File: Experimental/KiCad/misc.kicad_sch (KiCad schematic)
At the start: 72 parts, among them IC6 SN74LVC1G14DBVR, IC7 TPS62933ODRLR, IC8 TPS62933ODRLR, Q4 MMBT5401, Q5 2N7002, Q6 DMP3013SFV-7, Q7 DMP3013SFV-7, SW1 WBL2UOAGQR05CLR, SW2 LP4EE1RBATY, SW3 PEC16-2215F-S0024, X3 571-0400, X4 GSP1.9101.1, X5 PJ-002BH-SMT-TR

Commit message: BOM update, small changes
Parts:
- C22: TME R46KI310000M1M -> MKPX2-100NR15
- R34: TME SMD0603-3K3-1% -> SMD0603-200K-1%
- renumbered D9 to D10, D10 to D9, JP12 to JP13, R40 to R38, R38 to R39, R39 to R40
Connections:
- net +12P: now also D10.C
- net at C23.1, L1.1, TR1.V+ (+): no longer D10.C
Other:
- moved on the sheet: C32, D10, Q7, R38, X5, ZD2

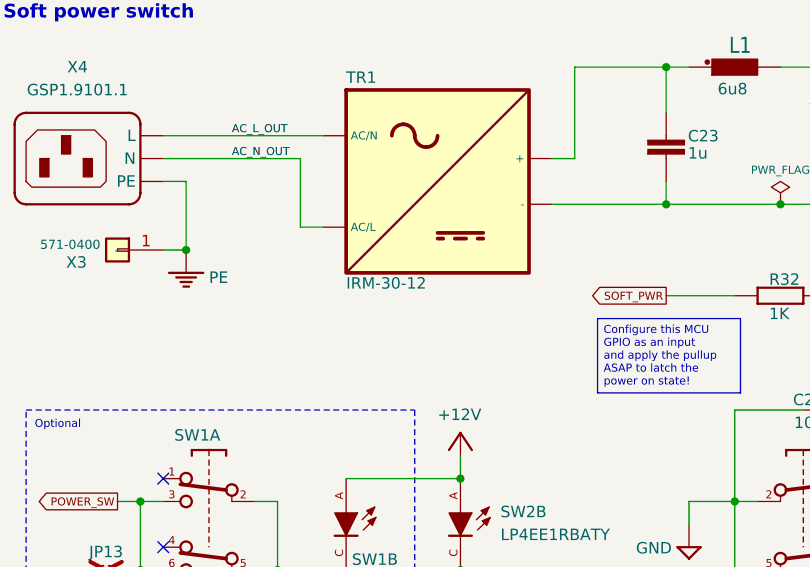
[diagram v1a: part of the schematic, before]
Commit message: AC/DC module replaced with 45/60W model
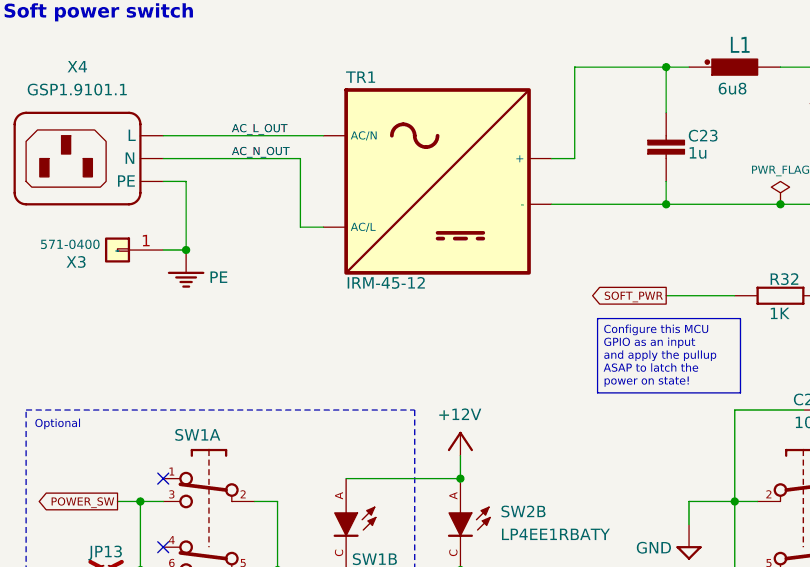
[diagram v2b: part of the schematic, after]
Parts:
- TR1: value IRM-30-12 -> IRM-45-12; footprint PCM_EEZ_THT:IRM-30 -> PCM_EEZ_THT:IRM-45; DigiKey 1866-3043-ND -> 1866-3053-ND; LCSC C193294 -> C5772350; Mouser 709-IRM30-12 -> 709-IRM45-12; TME IRM-30-12 -> IRM-45-12
- X5: Label (none) -> 12Vdc
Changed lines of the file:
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@@
+			)
+		)
+		(property "Label" "12Vdc"
+			(at 160.02 99.06 0)
+			(effects
+				(font
+					(size 0.889 0.889)
+				)
+				(hide yes)
 			)
 		)
@@
 			)
 		)
-		(property "Value" "IRM-30-12"
+		(property "Value" "IRM-45-12"
 			(at 53.34 47.625 0)
 			(effects
@@
 			)
 		)
-		(property "Footprint" "PCM_EEZ_THT:IRM-30"
+		(property "Footprint" "PCM_EEZ_THT:IRM-45"
 			(at 63.5 35.56 0)
 			(effects
@@
 			)
 		)
-		(property "DigiKey" "1866-3043-ND"
-			(at 63.5 35.56 0)
-			(effects
-				(font
-					(size 1.27 1.27)
-				)
-				(hide yes)
-			)
-		)
-		(property "Mouser" "709-IRM30-12"
-			(at 63.5 35.56 0)
-			(effects
-				(font
-					(size 1.27 1.27)
-				)
-				(hide yes)
-			)
-		)
-		(property "TME" "IRM-30-12"
-			(at 63.5 35.56 0)
-			(effects
-				(font
-					(size 1.27 1.27)
-				)
-				(hide yes)
-			)
-		)
-		(property "LCSC" "C193294"
-			(at 63.5 35.56 0)
-			(effects
+		(property "DigiKey" "1866-3053-ND"
+			(at 63.5 35.56 0)
+			(effects
+				(font
+					(size 1.27 1.27)
+				)
+				(hide yes)
+			)
+		)
+		(property "Mouser" "709-IRM45-12"
+			(at 63.5 35.56 0)
+			(effects
+				(font
+					(size 1.27 1.27)
+				)
+				(hide yes)
+			)
+		)
+		(property "TME" "IRM-45-12"
+			(at 63.5 35.56 0)
+			(effects
+				(font
+					(size 1.27 1.27)
+				)
+				(hide yes)
+			)
+		)
+		(property "LCSC" "C5772350"
+			(at 63.5 35.56 0)
+			(effects

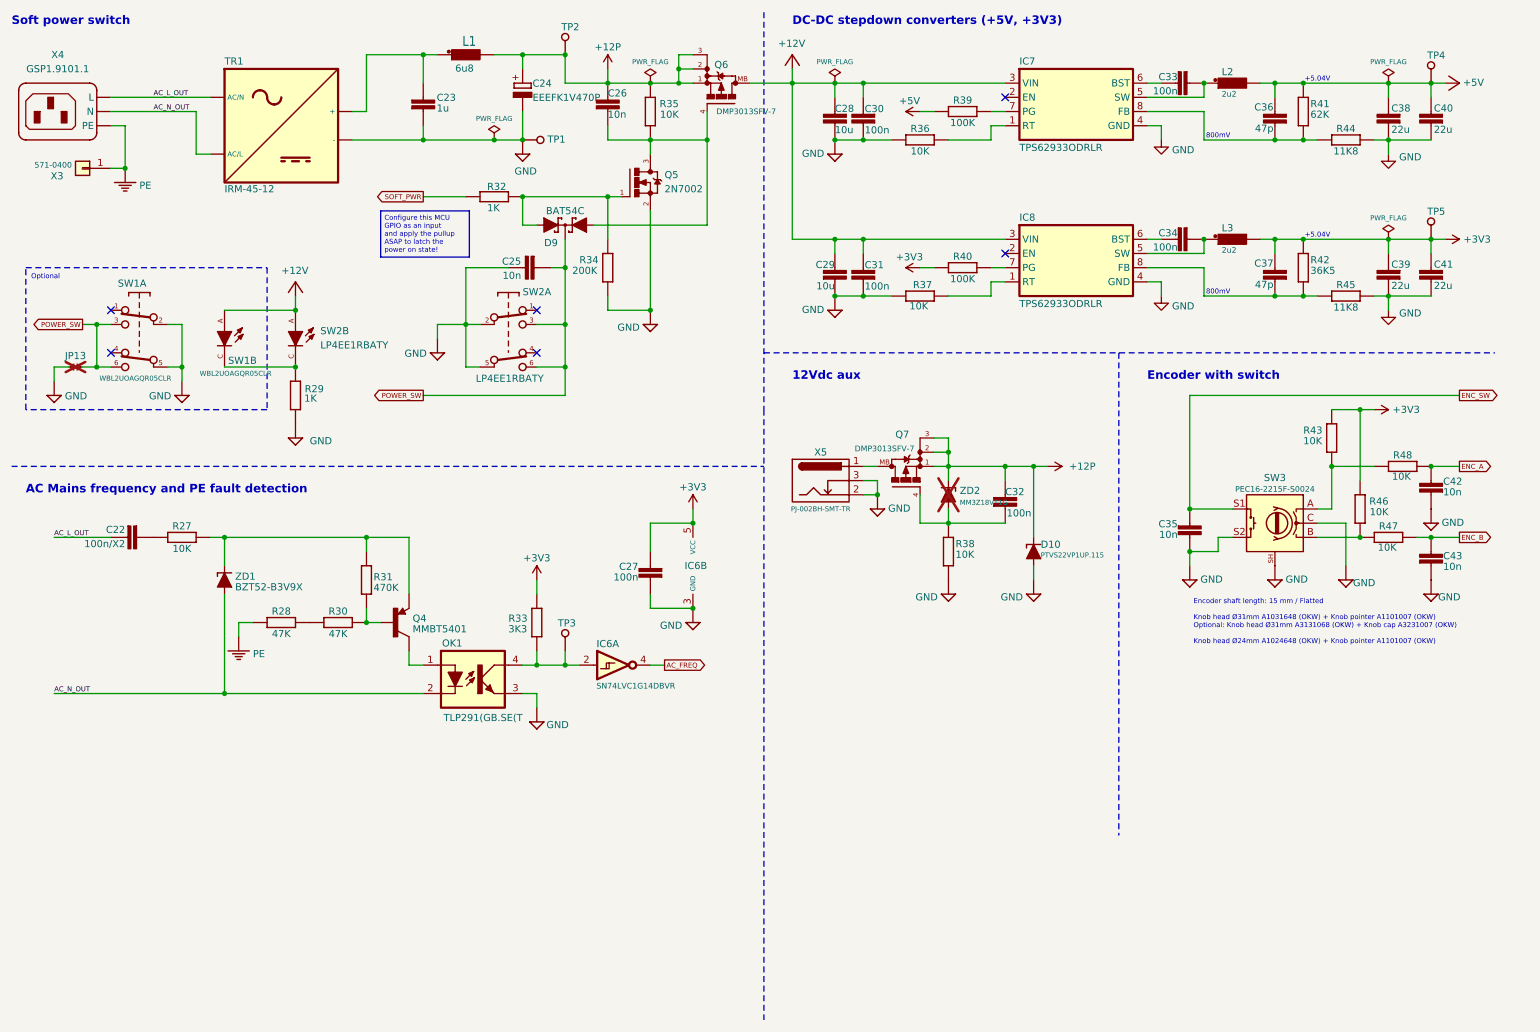
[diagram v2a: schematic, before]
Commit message: Replace 5V buck with 6A low EMI version
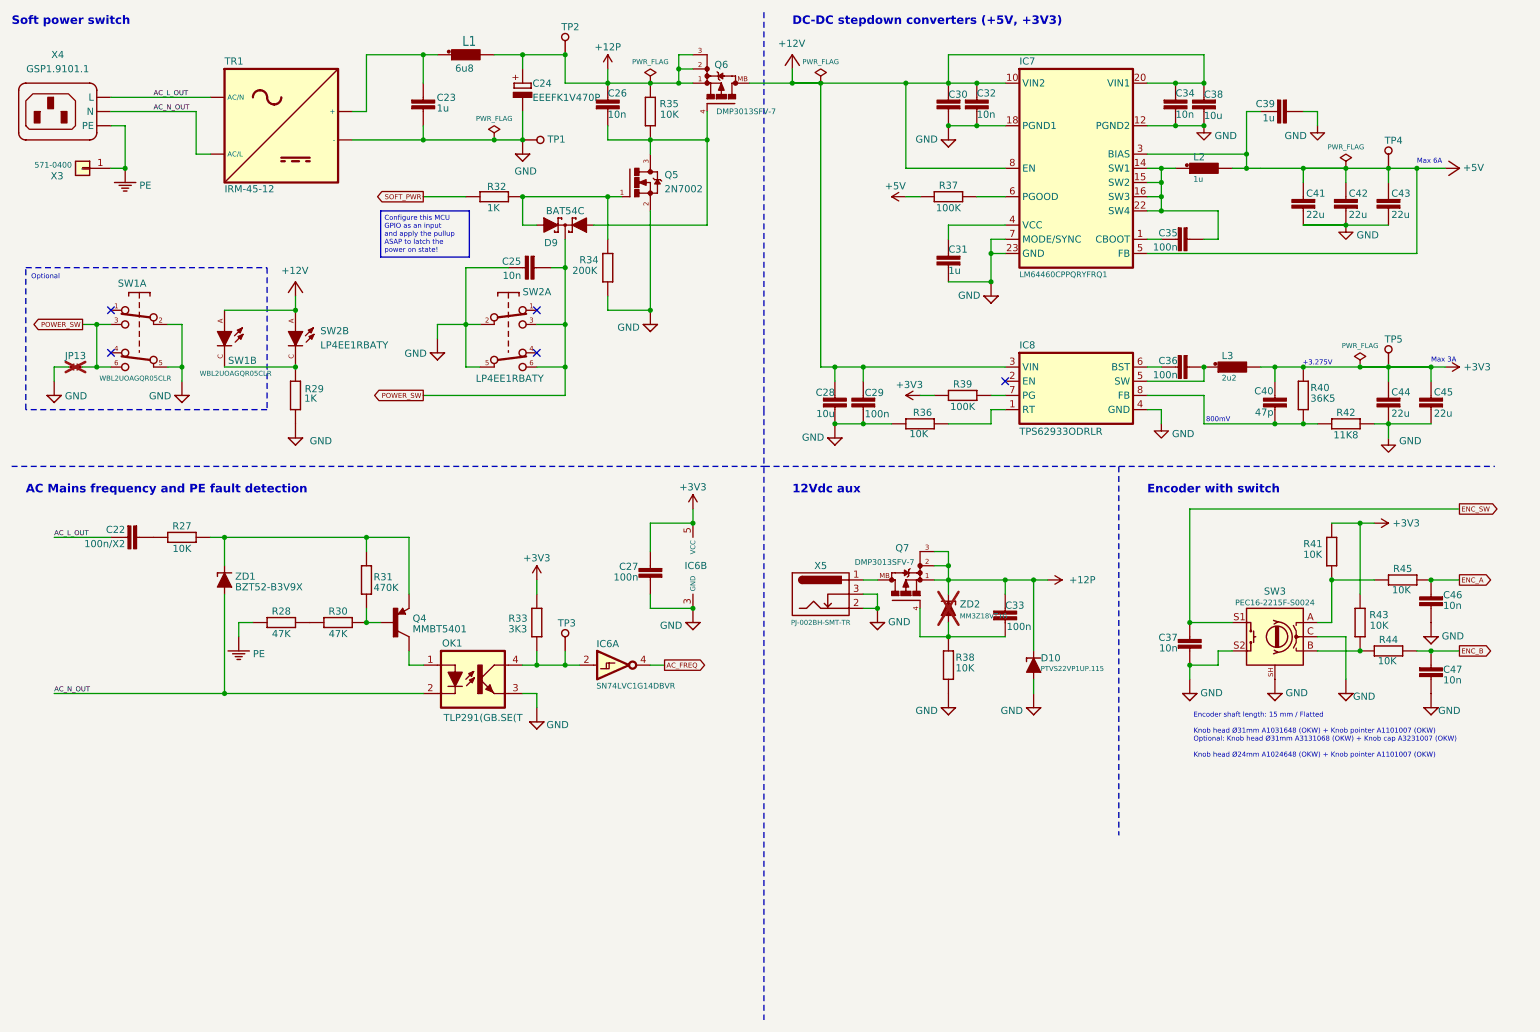
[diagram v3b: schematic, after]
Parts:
- removed C30: 100n, PCM_EEZ_passives:C_0603_1608Metric, symbol PCM_EEZ_passives:C-EU
- removed C36: 47p, PCM_EEZ_passives:C_0603_1608Metric, symbol PCM_EEZ_passives:C-EU
- removed R36: 10K, PCM_EEZ_passives:R_0603_1608Metric, symbol PCM_EEZ_passives:R-EU
- removed R41: 62K, PCM_EEZ_passives:R_0603_1608Metric, symbol PCM_EEZ_passives:R-EU
- removed R44: 11K8, PCM_EEZ_passives:R_0603_1608Metric, symbol PCM_EEZ_passives:R-EU
- added C31, C39: 1u, PCM_EEZ_passives:C_0603_1608Metric, symbol PCM_EEZ_passives:C-EU
- added C32, C34: 10n, PCM_EEZ_passives:C_0603_1608Metric, symbol PCM_EEZ_passives:C-EU
- added C38: 10u, PCM_EEZ_passives:C_0805_2012Metric, symbol PCM_EEZ_passives:C-EU
- added C43: 22u, PCM_EEZ_passives:C_0805_2012Metric, symbol PCM_EEZ_passives:C-EU
- IC7: value TPS62933ODRLR -> LM64460CPPQRYFRQ1; footprint PCM_EEZ_SMD:DRL0008A -> PCM_EEZ_SMD:VQFN22_RYF_TEX; symbol PCM_Uvitron:TPS62933ODRLR -> PCM_EEZ_TI:LM64460CPPQRYFRQ1; DigiKey 296-TPS62933ODRLRTR-ND -> 296-LM64460CPPQRYFRQ1CT-ND; LCSC C6290372 -> C34500172; Mouser 595-TPS62933ODRLR -> 595-LM64460CPPQRYFQ1
- IC8: symbol PCM_Uvitron:TPS62933ODRLR -> PCM_EEZ_TI:TPS62933ODRLR
- L2: value 2u2 -> 1u; DigiKey 118-SRP6030WA-2R2MCT-ND -> 118-SRP6030WA-1R0MCT-ND; LCSC C19947691 -> C19947689; Mouser 652-SRP6030WA-2R2M -> 652-SRP6030WA-1R0M
- renumbered C29 to C28, C31 to C29, C28 to C30, C32 to C33, C33 to C35, C34 to C36, C35 to C37, C37 to C40, C38 to C41, C40 to C42, C39 to C44, C41 to C45, C42 to C46, C43 to C47, R37 to R36, R39 to R37, R40 to R39, R42 to R40, R43 to R41, R45 to R42, R46 to R43, R47 to R44, R48 to R45
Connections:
- net +12V: now also IC7.10 (VIN2), IC7.20 (VIN1), IC7.8 (EN), C32.1, C34.1, C38.1; no longer IC7.3 (VIN)
- net +5V: now also IC7.3 (BIAS), IC7.5 (FB), C39.1, C43.2
- net GND: now also IC7.12 (PGND2), IC7.18 (PGND1), IC7.23 (GND), IC7.7 (MODE/SYNC), C31.2, C32.2, C34.2, C38.2, C39.2, C43.1; no longer IC7.4 (GND)
- net at IC7.1 (CBOOT): now also C35.1
- net at C35.2, L2.1: now also IC7.14 (SW1), IC7.15 (SW2), IC7.16 (SW3), IC7.22 (SW4); no longer IC7.5 (SW)
- net at IC7.6 (PGOOD): now also R37.1; no longer C35.1
- new net: C31.1, IC7.4 (VCC)
- no-connect marks 6 -> 5
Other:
- note added: "+3.275V"
- note added: "Max 3A"
- note added: "Max 6A"
- note removed: "+5.04V"
- moved on the sheet: C28, C29, C30, C33, C35, C36, C37, C40, C41, C42, C44, C45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

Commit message: Update project info
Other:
- company: Envox d.o.o. -> ${project_creator}
- title: BB3+ test mainboard -> ${project_name}
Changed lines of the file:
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@@
 	(paper "A4")
 	(title_block
-		(title "BB3+ test mainboard")
-		(date "2025-10-12")
-		(rev "r1B1")
-		(company "Envox d.o.o.")
-		(comment 1 "Licensed under the TAPR Open Hardware License (www.tapr.org/OHL)")
-		(comment 2 "More info at http://www.envox.eu/")
+		(title "${project_name}")
+		(date "2025-10-13")
+		(rev "${project_version}")
+		(company "${project_creator}")
+		(comment 1 "${project_license}")
+		(comment 2 "${project_info}")
 	)
 	(text "Encoder with switch"

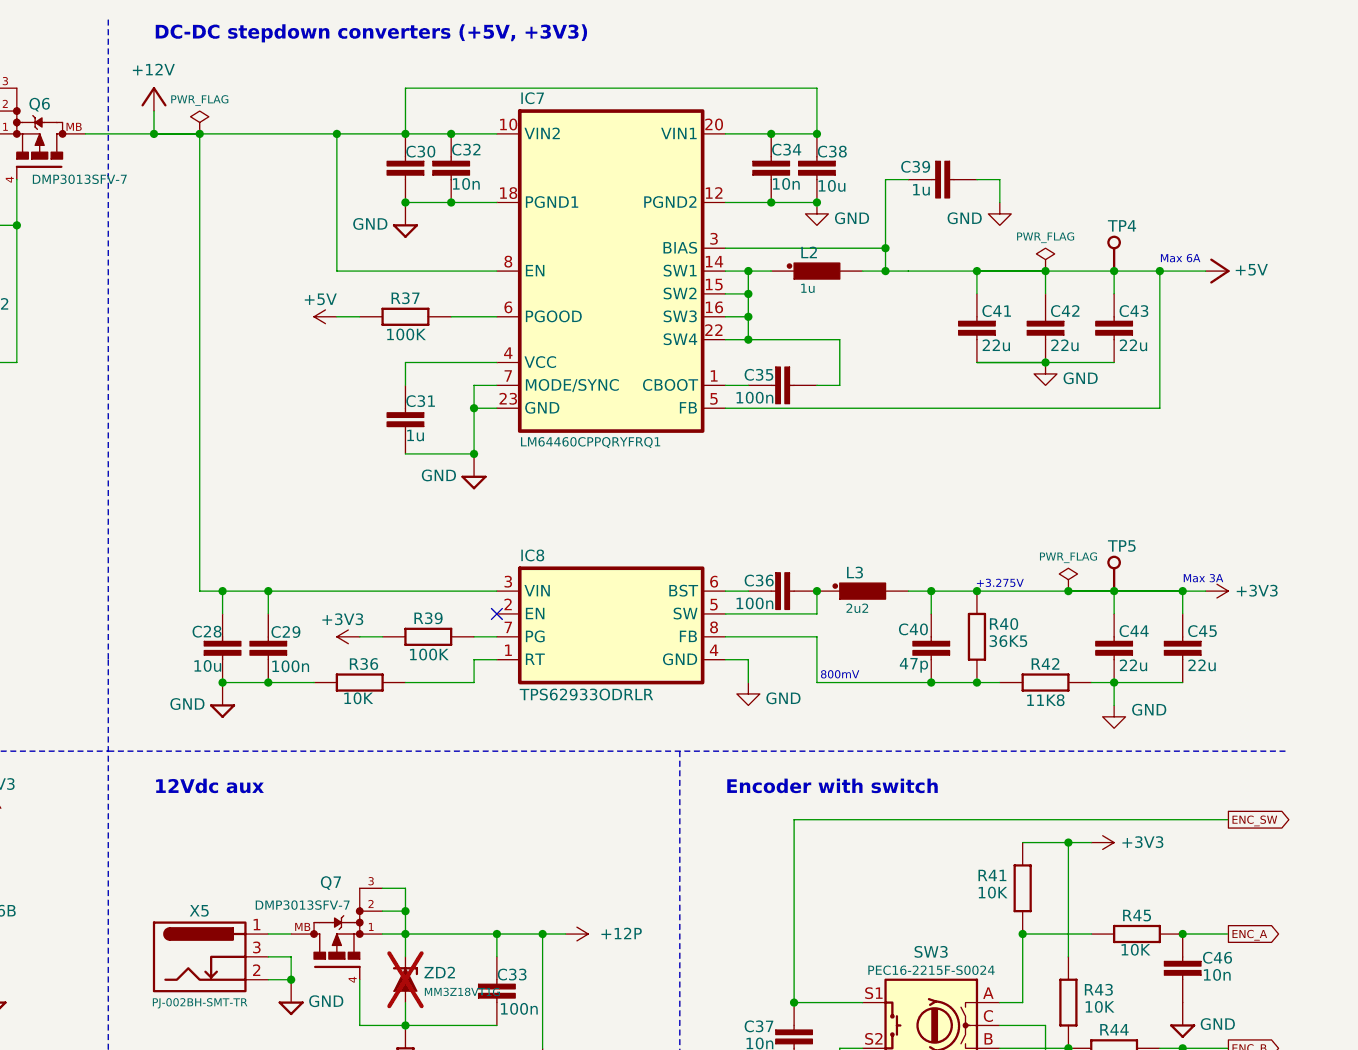
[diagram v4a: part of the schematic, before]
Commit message: Output LC filters added on all buck converters
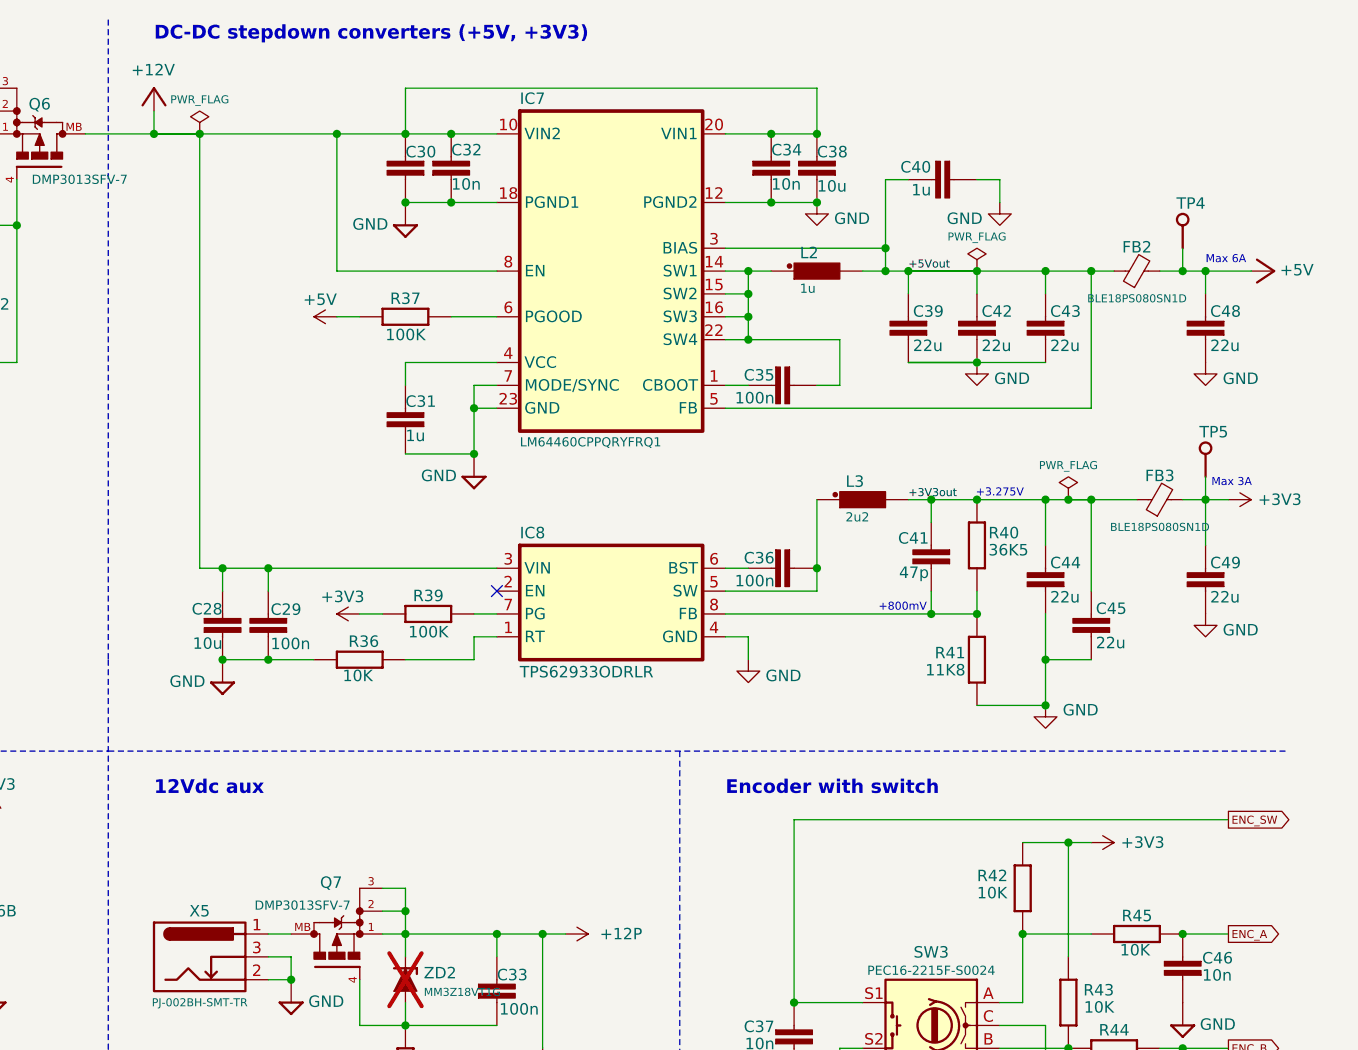
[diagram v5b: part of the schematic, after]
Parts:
- added C48, C49: 22u, PCM_EEZ_passives:C_0805_2012Metric, symbol PCM_EEZ_passives:C-EU
- added FB2, FB3: BLE18PS080SN1D, PCM_EEZ_passives:BEAD0603, symbol PCM_EEZ_passives:L_Ferrite Bead
- renumbered C41 to C39, C39 to C40, C40 to C41, R42 to R41, R41 to R42
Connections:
- net +3V3: now also C49.2, FB3.2; no longer C41.1, C44.2, C45.2, L3.2, R40.2
- net +5V: now also C48.2, FB2.2; no longer C39.2, C40.1, C42.2, C43.2, IC7.3 (BIAS), IC7.5 (FB), L2.2
- net GND: now also R41.2, C48.1, C49.1; no longer R41.1
- net at C41.2, IC8.8 (FB), R40.1: now also R41.1; no longer R41.2
- new net +3V3out: C41.1, C44.2, C45.2, FB3.1, L3.2, R40.2
- new net +5Vout: C39.2, C40.1, C42.2, C43.2, FB2.1, IC7.3 (BIAS), IC7.5 (FB), L2.2
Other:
- note added: "+800mV"
- note removed: "800mV"
- moved on the sheet: C28, C29, C36, C39, C41, C42, C43, C44, C45, IC8, L3, R36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

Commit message: Various small fixes
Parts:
- added LED5: LTST-C170KGKT, PCM_EEZ_SMD:LED_LTST-C170KGKT_LTO-L, symbol PCM_EEZ_discretes:DIODE_LED
- added R40: 1K8, PCM_EEZ_passives:R_0603_1608Metric, symbol PCM_EEZ_passives:R-EU
- renumbered R40 to R41, R41 to R42, R42 to R43, R43 to R44, R44 to R45, R45 to R46
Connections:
- net +12P: now also R40.2
- net GND: now also LED5.C
- new net: LED5.A, R40.1
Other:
- moved on the sheet: D10, R38
